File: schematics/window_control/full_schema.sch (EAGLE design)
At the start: 86 parts, among them IC1 MEGA32-P, J1 SERVO, Q1 2N3904, Q10 2N3906BU, Q11 2N3904, Q12 2N3906BU, Q13 2N3904, Q14 2N3904, Q16 2N3906BU, Q17 STP14NM50N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

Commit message: Continue working under schematics
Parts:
- removed R21, R23: 10K, my_devices:R
- added Q5: 2N3904, my_devices:TRANSISTOR_NPN
- added R16: 200, my_devices:R
- added R20: 150K, my_devices:R
- added U10: LM311P, my_devices:LM311P
- C17: value C-1 -> 5nF
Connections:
- removed net 3V3: U1.3V3
- new net N$37: Q16.B, Q5.C
- new net N$50: Q5.B, U10.EMI_OUT
- new net N$53: C17.P$2, R20.P$1, U10.IN+
- net +5V: now also R20.P$2, U10.IN-, U10.VCC; no longer R21.P$1, R23.P$2
- net GND: now also R16.P$2, U10.GND
- net N$38: now also Q5.E, R16.P$1; no longer C17.P$1, Q16.B, R21.P$2
- net SERVO_PWM_CONTROL: now also C17.P$1; no longer C17.P$2, R23.P$1
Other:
- moved on the sheet: C17

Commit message: continue working under schematics
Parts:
- removed Q6: (no value), my_devices:TRANSISTOR_PNP
- removed R17: 10K, my_devices:R
- C18: value 10uF -> C
- C19: value 1 nF -> 4.7 nF
- C20: value C-1 -> 80 pF
- R4: value 10K -> R
- R5: value 10K -> 100
- R7: value RD -> 20K
- R8: value R -> 100
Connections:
- removed net N$52: Q6.B, R17.P$1, U8.OUT
- new net +5V_IF_EN: C18.PIN_PLUS, L4.P$1, Q16.C, R4.P$1, R8.P$2, U8.RESET, U8.VCC
- net +5V: no longer L4.P$1, Q6.E, R17.P$2
- net GND: no longer R5.P$1
- net N$35: now also R5.P$1, U8.OUT; no longer Q4.B, Q6.C, R5.P$2
- net N$43: now also Q4.B, R5.P$2; no longer C18.PIN_PLUS, Q16.C, R4.P$1, R8.P$2, U8.RESET, U8.VCC
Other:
- note added: "~10-20V max 50 mA"
- moved on the sheet: C16, C18, C19, C20, D7, D8, D9, J1, L4, Q17, Q4, R4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

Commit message: working under schematics
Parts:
- added Q6, Q7: 2N3904, my_devices:TRANSISTOR_NPN
- added R17, R21, R22: 1K, my_devices:R
- C18: value C -> 1000 uF
- C19: value 4.7 nF -> 10 pF
- R4: value R -> 1K
- R6: value 4K -> 3K
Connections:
- removed net SERVO_IS_ENABLED_INV: R12.P$2
- new net 3V3: R21.P$1, R22.P$1, U1.3V3
- new net HALL_IS_ENABLED: Q6.C, R12.P$2, R21.P$2
- new net N$52: U9.3A, U9.4Y
- new net N$54: Q6.B, R4.P$2
- new net N$55: Q7.B, R17.P$2
- new net SW_IS_ON: Q7.C, R19.P$2, R22.P$2
- net +5V_IF_EN: no longer R4.P$1
- net GND: now also Q6.E, Q7.E, U9.1B; no longer R4.P$2
- net HALL_OUT_INV: no longer R19.P$2
- net N$1: now also R17.P$1
- net N$3: now also R4.P$1, U9.4B; no longer U9.3B
- net SERVO_ENABLE_INV: now also U9.4A; no longer U9.1B
- net SERVO_PWM: now also U9.3B; no longer U9.3A
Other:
- note added: "Check temperature of this transistor!"
- note added: "~10-15-20V In my case ~12V Mosfet needs >8V"
- note removed: "~10-20V max 50 mA"
- moved on the sheet: B1, C18, C20, D1, Q1, Q2, Q3, R1, R10, R11, R12, R19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

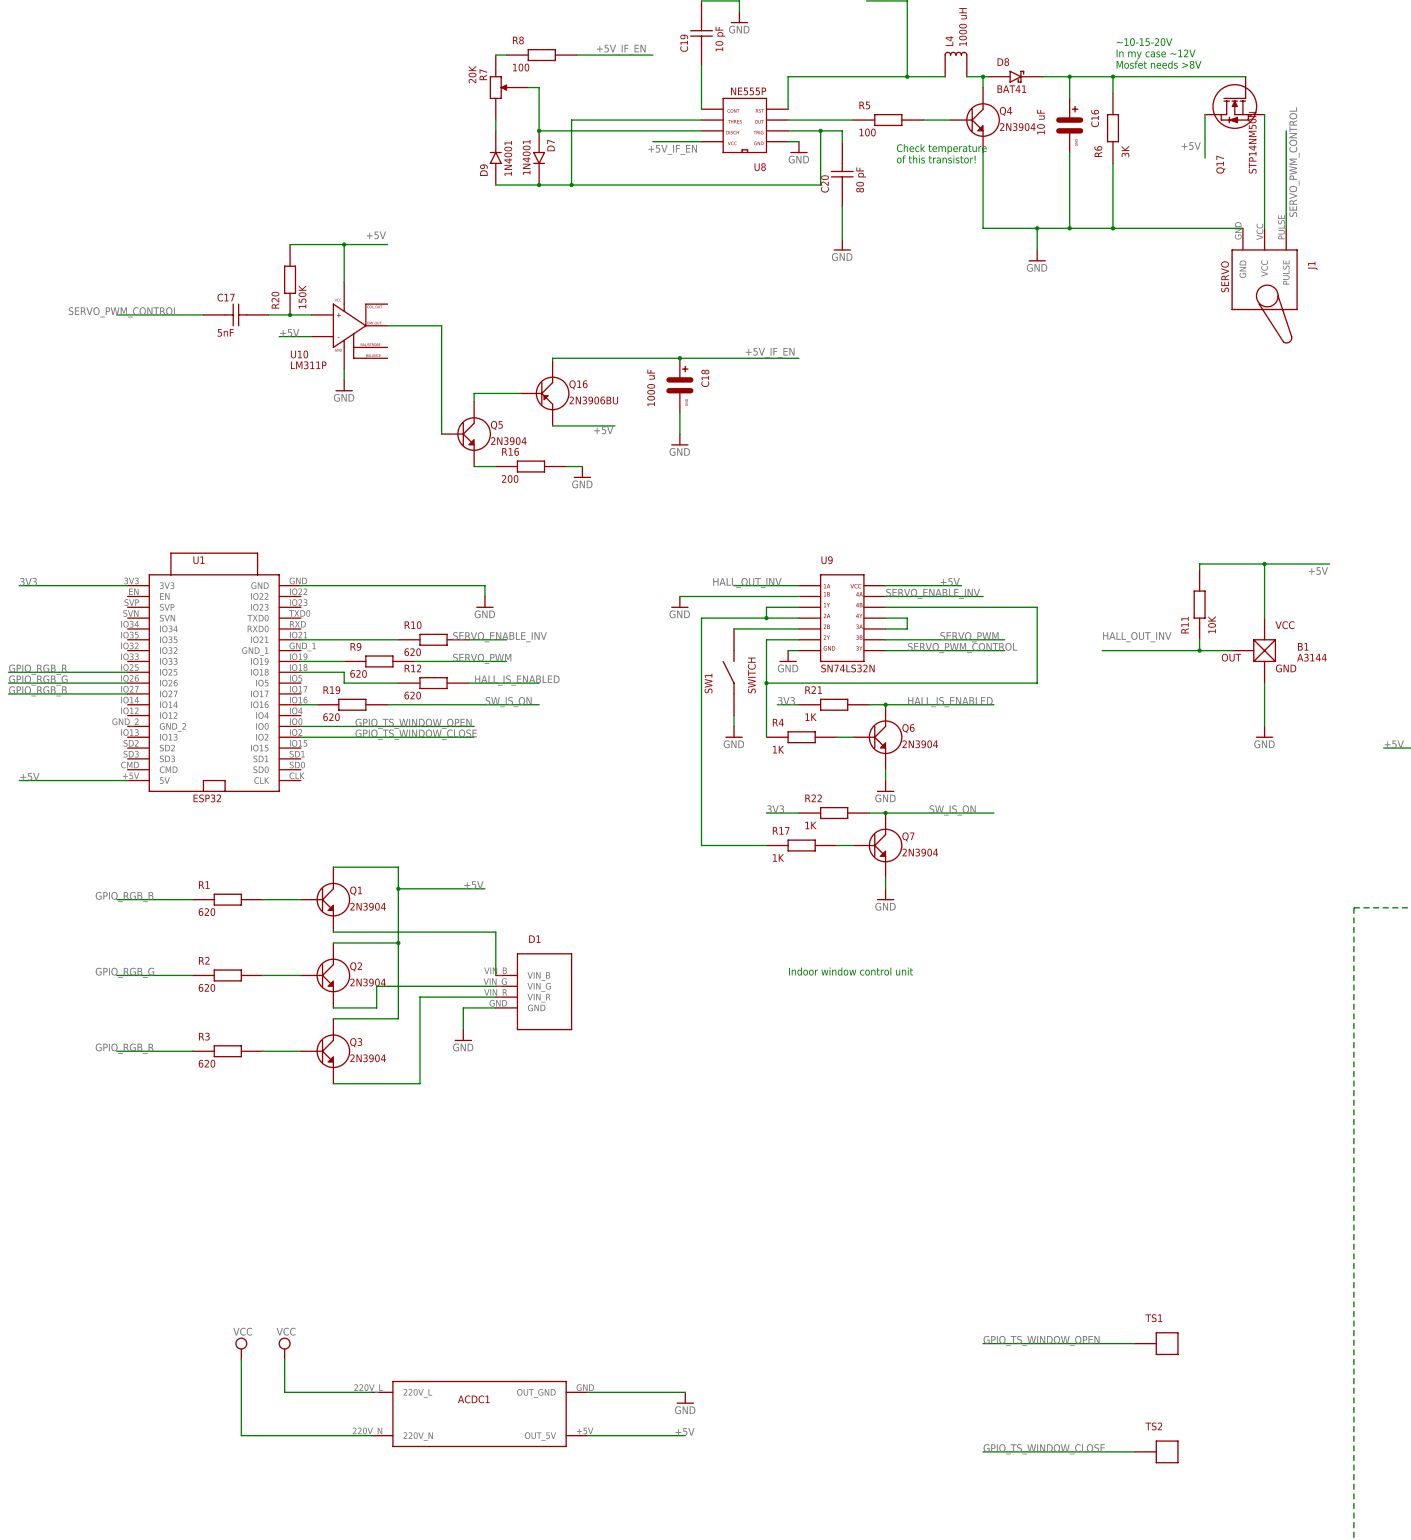
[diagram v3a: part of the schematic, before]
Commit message: 1. working under schematics. 2. ESP32 firmware writen but not tested yet. 3. I conntected to ATMega controller and uploaded test firmware to it
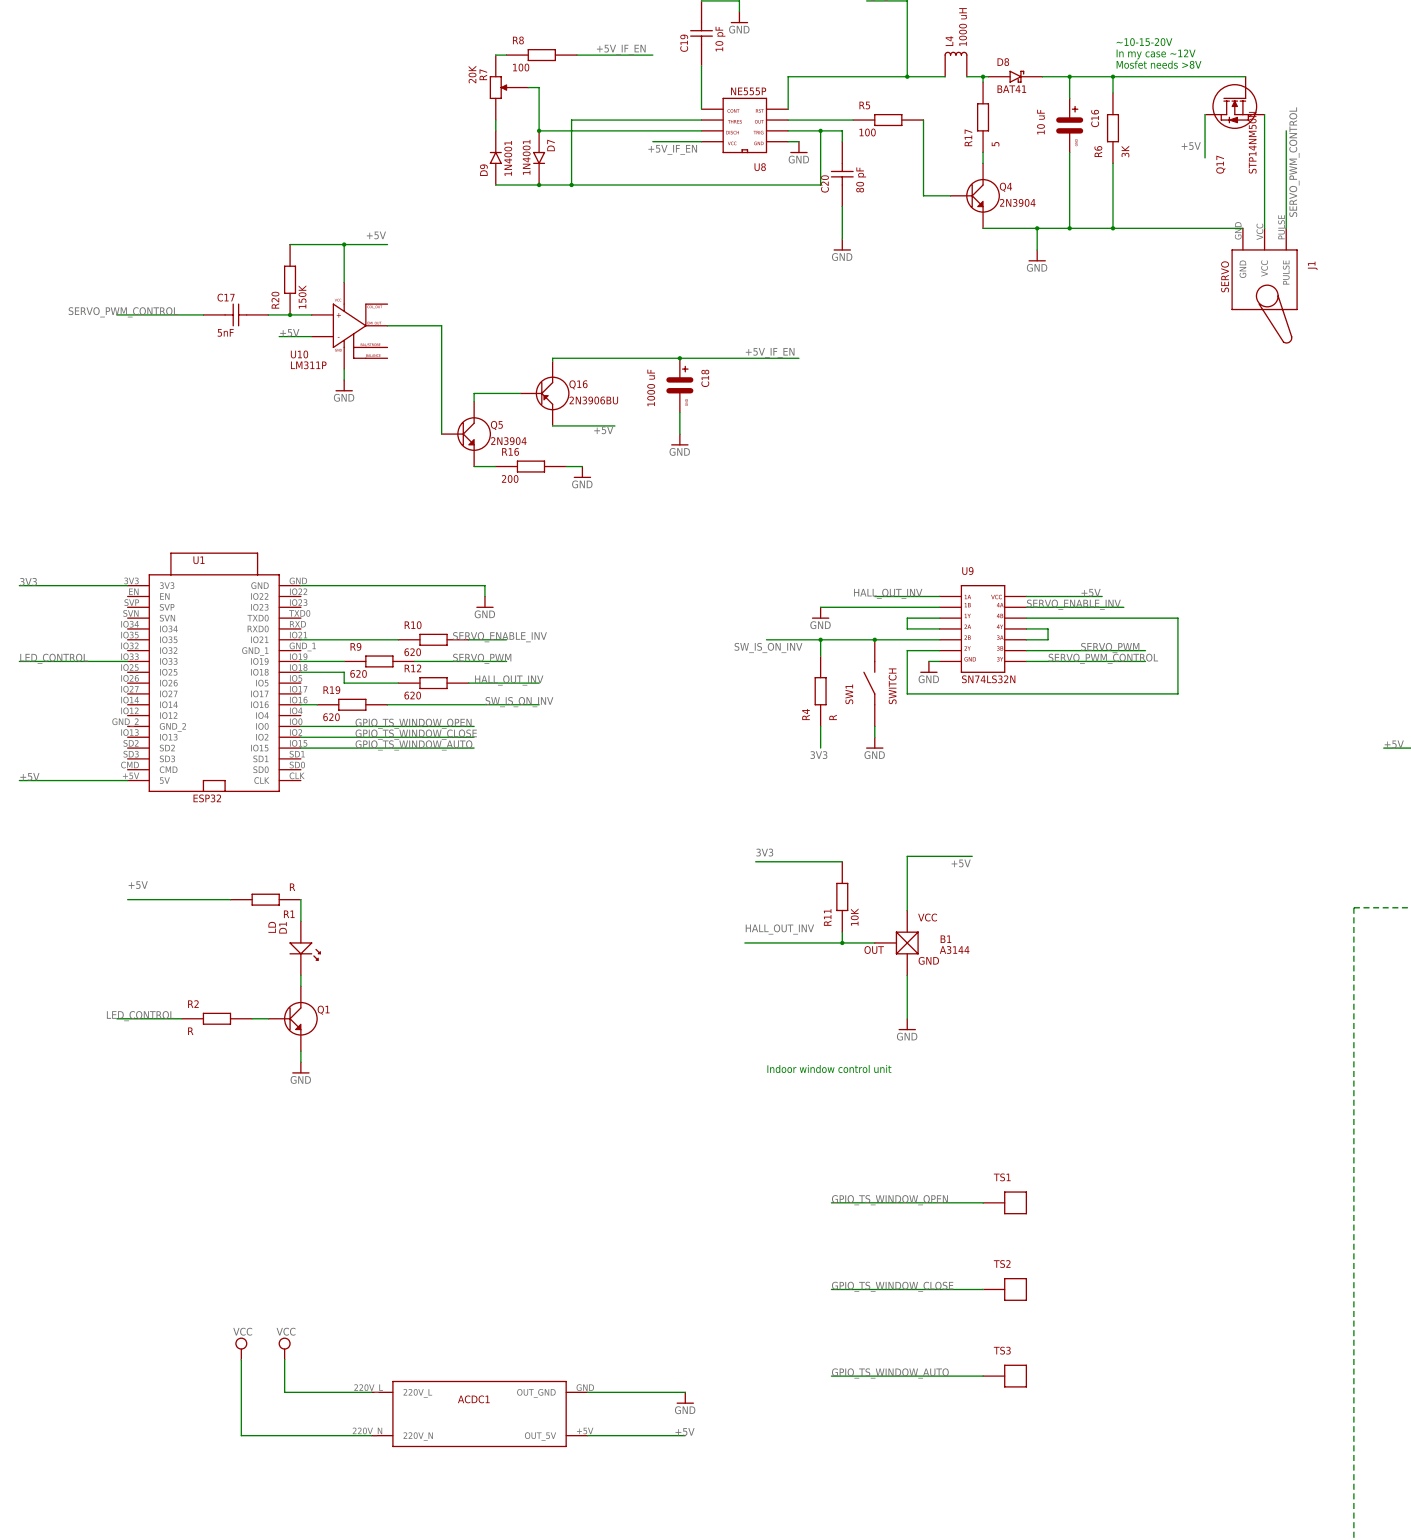
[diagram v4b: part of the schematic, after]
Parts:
- removed Q2, Q3, Q6, Q7: 2N3904, my_devices:TRANSISTOR_NPN
- removed R21, R22: 1K, my_devices:R
- removed R3: 620, my_devices:R
- added TS3: TOUCH_SENSOR, my_devices:TOUCH_SENSOR
- D1: value RGBLED -> LD; device my_devices:RGBLED -> my_devices:LD
- Q1: value 2N3904 -> (none)
- R1, R2: value 620 -> R
- R17: value 1K -> 5
- R4: value 1K -> R
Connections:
- removed net GPIO_RGB_B: R1.P$1, U1.IO27
- removed net GPIO_RGB_G: R2.P$1, U1.IO26
- removed net GPIO_RGB_R: R3.P$1, U1.IO25
- removed net HALL_IS_ENABLED: Q6.C, R12.P$2, R21.P$2
- removed net N$2 (its old number): SW1.P$2, U9.2B
- removed net N$21: Q1.B, R1.P$2
- removed net N$22: Q2.B, R2.P$2
- removed net N$23: Q3.B, R3.P$2
- removed net N$54: Q6.B, R4.P$2
- removed net N$55: Q7.B, R17.P$2
- removed net SW_IS_ON: Q7.C, R19.P$2, R22.P$2
- new net GPIO_TS_WINDOW_AUTO: TS3.P$1, U1.IO15
- new net LED_CONTROL: R2.P$1, U1.IO33
- new net N$56: U9.1Y, U9.2A
- new net SW_IS_ON_INV: R19.P$2, R4.P$2, SW1.P$2, U9.2B
- net +5V: now also R1.P$2; no longer Q1.C, Q2.C, Q3.C, R11.P$2
- net 3V3: now also R11.P$2, R4.P$1; no longer R21.P$1, R22.P$1
- net GND: now also Q1.E; no longer D1.GND, Q6.E, Q7.E
- net HALL_OUT_INV: now also R12.P$2
- net N$1: now also Q4.C; no longer U9.1Y, U9.2A
- net N$3: no longer R4.P$1
- net N$39: now also R17.P$2; no longer Q4.C
- net N$5: now also Q1.B, R2.P$2; no longer D1.VIN_B, Q1.E
- net N$7: now also D1.PIN_ANODE, Q1.C; no longer D1.VIN_G, Q2.E
- net N$8: now also D1.PIN_CATHODE, R1.P$1; no longer D1.VIN_R, Q3.E
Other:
- note removed: "Check temperature of this transistor!"
- moved on the sheet: B1, Q1, Q4, R1, R11, R17, R2, R4, SW1, TS1, TS2, U9

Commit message: Start debugging process
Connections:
- net GPIO_TS_WINDOW_AUTO: now also U1.IO12; no longer U1.IO15
- net GPIO_TS_WINDOW_CLOSE: now also U1.IO27; no longer U1.IO2
- net GPIO_TS_WINDOW_OPEN: now also U1.IO14; no longer U1.IO0
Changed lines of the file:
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@@
 </segment>
 <segment>
-<pinref part="U1" gate="G$1" pin="IO0"/>
-<wire x1="-195.58" y1="116.84" x2="-154.94" y2="116.84" width="0.1524" layer="91" grouprefs="ESP"/>
-<label x="-182.88" y="116.84" size="1.778" layer="95" grouprefs="ESP"/>
+<pinref part="U1" gate="G$1" pin="IO14"/>
+<wire x1="-236.22" y1="121.92" x2="-261.62" y2="121.92" width="0.1524" layer="91" grouprefs="ESP"/>
+<label x="-274.32" y="121.92" size="1.778" layer="95" grouprefs="ESP"/>
 </segment>
 </net>
@@
 </segment>
 <segment>
-<pinref part="U1" gate="G$1" pin="IO2"/>
-<wire x1="-195.58" y1="114.3" x2="-154.94" y2="114.3" width="0.1524" layer="91" grouprefs="ESP"/>
-<label x="-182.88" y="114.3" size="1.778" layer="95" grouprefs="ESP"/>
+<pinref part="U1" gate="G$1" pin="IO27"/>
+<wire x1="-236.22" y1="124.46" x2="-261.62" y2="124.46" width="0.1524" layer="91" grouprefs="ESP"/>
+<label x="-274.32" y="124.46" size="1.778" layer="95" grouprefs="ESP"/>
 </segment>
 </net>
@@
 </segment>
 <segment>
-<pinref part="U1" gate="G$1" pin="IO15"/>
-<wire x1="-195.58" y1="111.76" x2="-154.94" y2="111.76" width="0.1524" layer="91"/>
-<label x="-182.88" y="111.76" size="1.778" layer="95"/>
-</segment>
-</net>
+<pinref part="U1" gate="G$1" pin="IO12"/>
+<wire x1="-236.22" y1="119.38" x2="-261.62" y2="119.38" width="0.1524" layer="91" grouprefs="ESP"/>
+<label x="-274.32" y="119.38" size="1.778" layer="95" grouprefs="ESP"/>
+</segment>
+</net>

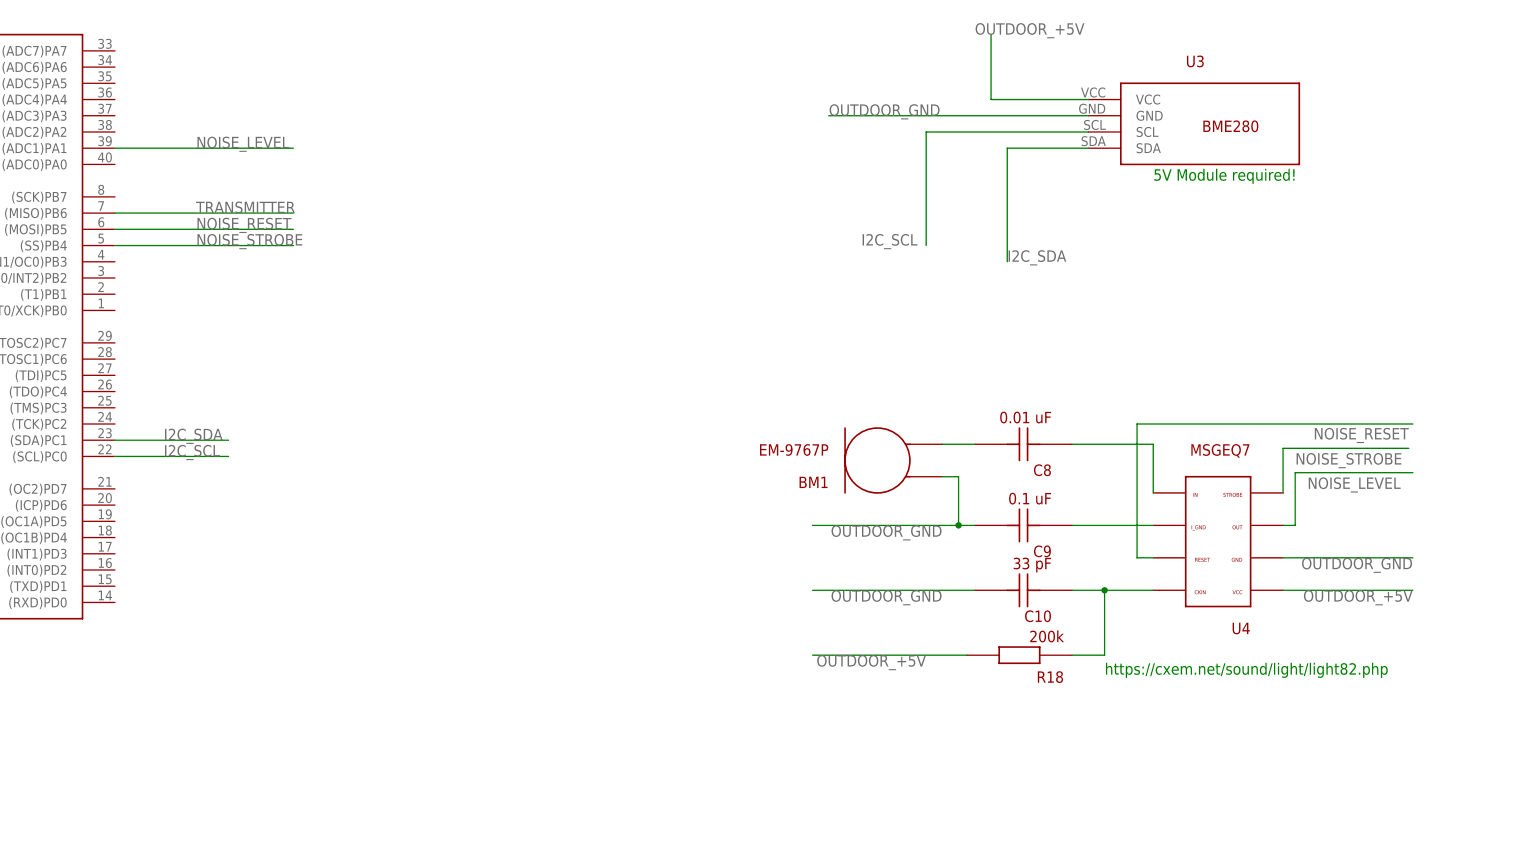
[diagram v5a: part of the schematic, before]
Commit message: SGP30 Module works now
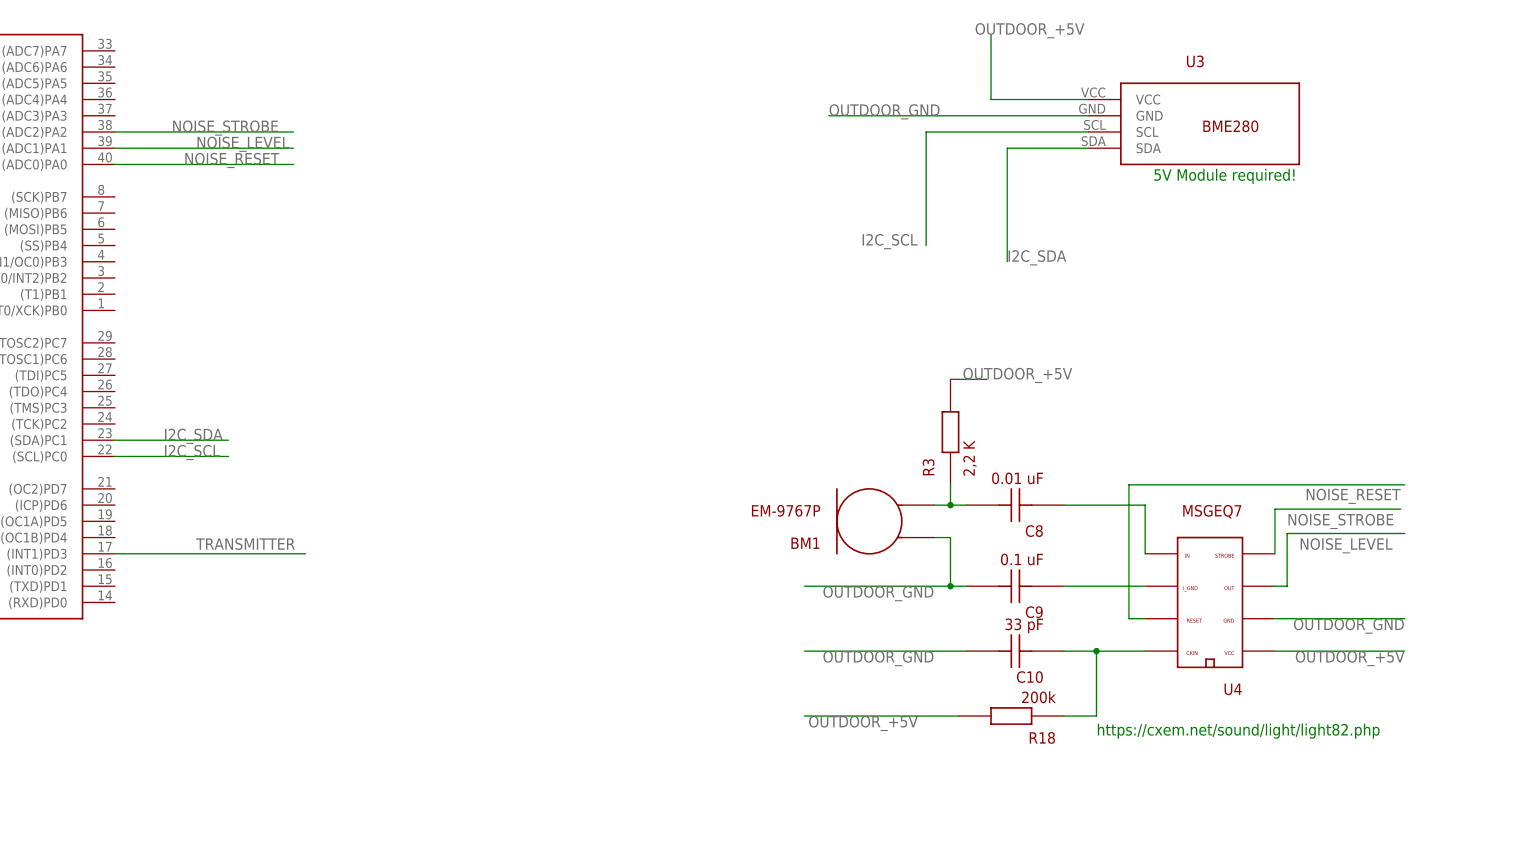
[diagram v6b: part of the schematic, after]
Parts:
- added R3: 2,2 K, my_devices:R
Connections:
- removed net N$20: BM1.P$2, C8.P$2
- new net N$21: BM1.P$2, C8.P$2, R3.P$1
- net NOISE_RESET: now also IC1.(ADC0)PA0; no longer IC1.(MOSI)PB5
- net NOISE_STROBE: now also IC1.(ADC2)PA2; no longer IC1.(SS)PB4
- net OUTDOOR_+5V: now also R3.P$2
- net TRANSMITTER: now also IC1.(INT1)PD3; no longer IC1.(MISO)PB6
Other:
- moved on the sheet: BM1, C10, C8, C9, R18
